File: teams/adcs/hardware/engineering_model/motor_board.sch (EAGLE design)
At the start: 80 parts

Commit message: Slight tweaks and initial board organization
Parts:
- removed BRAKE_MODE, COMMUTATION_MODE, DRIVE_ANGLE: (no value), SparkFun-Connectors:CONN_03LOCK
- removed C1: 2.2uF, rcl:C-USC1206
- removed C2, C4: 0.1uF, rcl:C-USC0805
- removed C3, C5: 1uF, rcl:C-USC1206
- removed MOTOR, MOTOR1, MOTOR2, MOTOR3: (no value), SparkFun-Connectors:CONN_08"
- removed R1, R2, R3, R4: 3.3K, rcl:R-US_R0805
- removed R5, R6, R7: 10K, rcl:R-US_R0805
- removed R8: (no value), rcl:R-US_R0805
- removed U$9: DRV10970, DubSat1 Components:DRV10970
- added MOTOR_X, MOTOR_Y, MOTOR_Z: PICOLOCK_8, DubSat1 Components:PICOLOCK_8
- renumbered BRKMOD_X1 to BRKMOD_Y, BRKMOD_X2 to BRKMOD_Z, CMTMOD_X1 to CMTMOD_Y, CMTMOD_X2 to CMTMOD_Z, DAA_X1 to DAA_Y, DAA_X2 to DAA_Z
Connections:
- removed net N$19: C1.1, U$9.RETRY
- removed net N$26: R1.1, U$9.RD
- removed net N$27: R2.2, U$9.FG
- removed net N$28: U$9.FR
- removed net N$29: C3.2, U$9.VCP
- removed net N$31: R3.2, R4.1, U$9.U_HN, U$9.V_HN, U$9.W_HN
- removed net N$32: DRIVE_ANGLE.2, U$9.DAA
- removed net N$33: COMMUTATION_MODE.2, U$9.CMTMOD
- removed net N$34: BRAKE_MODE.2, U$9.BRKMOD
- removed net N$35: BRAKE_MODE.3, C4.2, COMMUTATION_MODE.3, DRIVE_ANGLE.3, MOTOR.5, R1.2, R2.1, R4.2, R5.1, R6.1, R7.1, U$9.VINT
- removed net N$37: C2.2, U$9.CPP
- removed net N$42: C2.1, U$9.CPN
- removed net N$43: MOTOR.1, U$9.W
- removed net N$44: MOTOR.2, U$9.V
- removed net N$45: MOTOR.6, R7.2, U$9.W_HP
- removed net N$46: MOTOR.7, R6.2, U$9.V_HP
- removed net N$47: MOTOR.8, R5.2, U$9.U_HP
- removed net N$48: R8.2, U$9.CS
- removed net N$49: MOTOR.3, U$9.U
- removed net N$56: C5.2, U$9.VM
- net GND: now also MOTOR_X.P$4, MOTOR_Y.P$4, MOTOR_Z.P$4; no longer BRAKE_MODE.1, C1.2, C3.1, C4.1, C5.1, COMMUTATION_MODE.1, DRIVE_ANGLE.1, MOTOR.4, MOTOR1.4, MOTOR2.4, MOTOR3.4, R3.1, R8.1, U$9.GND
- net N$23: now also MOTOR_Y.P$1; no longer MOTOR2.1
- net N$25: now also MOTOR_Y.P$2; no longer MOTOR2.2
- net N$40: now also MOTOR_Y.P$6; no longer MOTOR2.6
- net N$41: now also MOTOR_Y.P$7; no longer MOTOR2.7
- net N$52: now also MOTOR_X.P$1; no longer MOTOR1.1
- net N$53: now also MOTOR_X.P$2; no longer MOTOR1.2
- net N$54: now also MOTOR_X.P$6; no longer MOTOR1.6
- net N$55: now also MOTOR_X.P$7; no longer MOTOR1.7
- net N$57: now also MOTOR_X.P$8; no longer MOTOR1.8
- net N$59: now also MOTOR_X.P$3; no longer MOTOR1.3
- net N$60: now also MOTOR_Y.P$8; no longer MOTOR2.8
- net N$62: now also MOTOR_Y.P$3; no longer MOTOR2.3
- net N$77: now also MOTOR_Z.P$1; no longer MOTOR3.1
- net N$78: now also MOTOR_Z.P$2; no longer MOTOR3.2
- net N$79: now also MOTOR_Z.P$6; no longer MOTOR3.6
- net N$80: now also MOTOR_Z.P$7; no longer MOTOR3.7
- net N$81: now also MOTOR_Z.P$8; no longer MOTOR3.8
- net N$83: now also MOTOR_Z.P$3; no longer MOTOR3.3
- net VINT_X: now also MOTOR_X.P$5; no longer MOTOR1.5
- net VINT_Y: now also MOTOR_Y.P$5; no longer MOTOR2.5
- net VINT_Z: now also MOTOR_Z.P$5; no longer MOTOR3.5

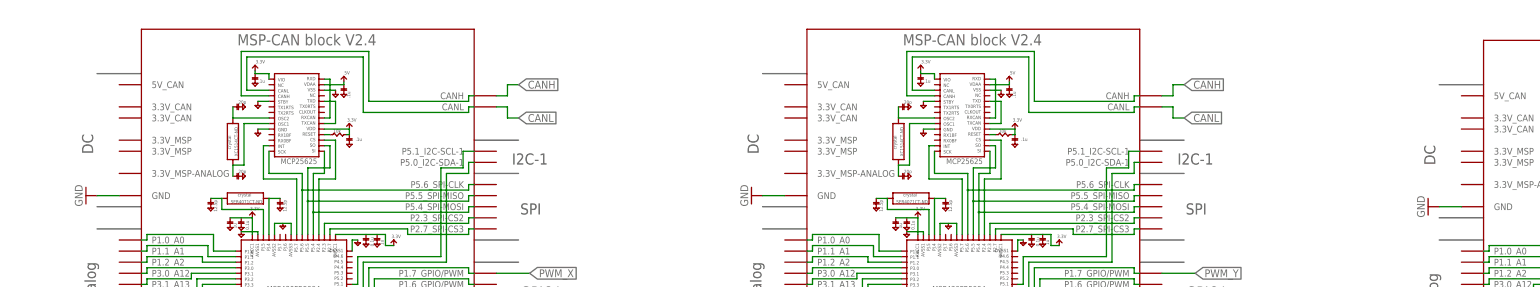
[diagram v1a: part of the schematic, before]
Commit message: ADCS/RW - Added voltage nets for MCU regulators
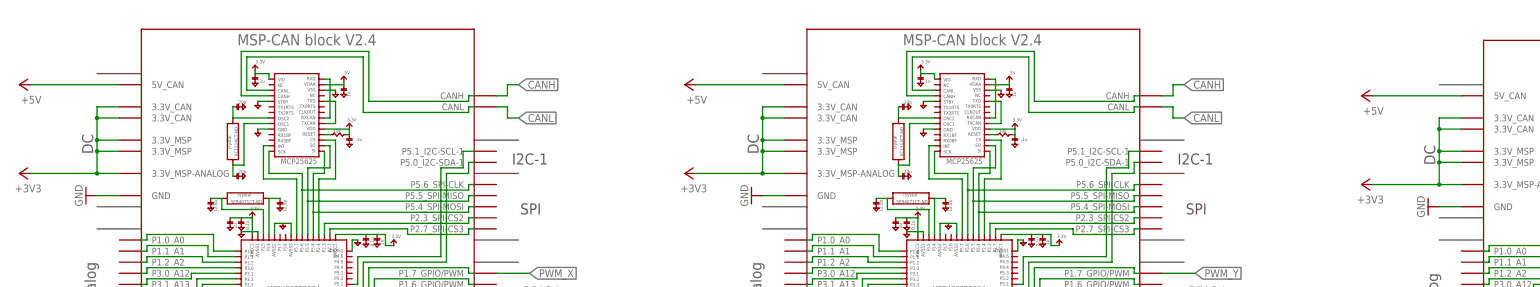
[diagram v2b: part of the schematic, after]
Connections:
- new net +3V3: U$3.3.3V_CAN@1, U$3.3.3V_CAN@2, U$3.3.3V_MSP-ANALOG@1, U$3.3.3V_MSP@2, U$3.3.3V_MSP@3
- new net +5V: U$3.5V_CAN
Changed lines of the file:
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@@
 <?xml version="1.0" encoding="utf-8"?>
 <!DOCTYPE eagle SYSTEM "eagle.dtd">
-<eagle version="8.3.1">
+<eagle version="8.3.2">
 <drawing>
 <settings>
@@
 <part name="MOTOR_Y" library="DubSat1 Components" deviceset="PICOLOCK_8" device=""/>
 <part name="MOTOR_Z" library="DubSat1 Components" deviceset="PICOLOCK_8" device=""/>
+<part name="+3V1" library="supply1" library_urn="urn:adsk.eagle:library:371" deviceset="+3V3" device=""/>
+<part name="P+1" library="supply1" library_urn="urn:adsk.eagle:library:371" deviceset="+5V" device=""/>
+<part name="+3V2" library="supply1" library_urn="urn:adsk.eagle:library:371" deviceset="+3V3" device=""/>
+<part name="P+2" library="supply1" library_urn="urn:adsk.eagle:library:371" deviceset="+5V" device=""/>
+<part name="+3V3" library="supply1" library_urn="urn:adsk.eagle:library:371" deviceset="+3V3" device=""/>
+<part name="P+3" library="supply1" library_urn="urn:adsk.eagle:library:371" deviceset="+5V" device=""/>
 </parts>
 <sheets>
@@
 <instance part="MOTOR_Y" gate="G$1" x="154.94" y="-157.48"/>
 <instance part="MOTOR_Z" gate="G$1" x="309.88" y="-160.02"/>
+<instance part="+3V1" gate="G$1" x="-63.5" y="-55.88" rot="R90"/>
+<instance part="P+1" gate="1" x="-63.5" y="-35.56" rot="R90"/>
+<instance part="+3V2" gate="G$1" x="88.9" y="-55.88" rot="R90"/>
+<instance part="P+2" gate="1" x="88.9" y="-35.56" rot="R90"/>
+<instance part="+3V3" gate="G$1" x="243.84" y="-58.42" rot="R90"/>
+<instance part="P+3" gate="1" x="243.84" y="-38.1" rot="R90"/>
 </instances>
 <busses>
@@
 </segment>
 </net>
+<net name="+3V3" class="0">
+<segment>
+<pinref part="+3V1" gate="G$1" pin="+3V3"/>
+<pinref part="U$3" gate="G$1" pin="3.3V_MSP-ANALOG@1"/>
+<wire x1="-60.96" y1="-55.88" x2="-45.72" y2="-55.88" width="0.1524" layer="91"/>
+<pinref part="U$3" gate="G$1" pin="3.3V_MSP@2"/>
+<wire x1="-45.72" y1="-55.88" x2="-40.64" y2="-55.88" width="0.1524" layer="91"/>
+<wire x1="-45.72" y1="-55.88" x2="-45.72" y2="-50.8" width="0.1524" layer="91"/>
+<wire x1="-45.72" y1="-50.8" x2="-40.64" y2="-50.8" width="0.1524" layer="91"/>
+<junction x="-45.72" y="-55.88"/>
+<pinref part="U$3" gate="G$1" pin="3.3V_MSP@3"/>
+<wire x1="-45.72" y1="-50.8" x2="-45.72" y2="-48.26" width="0.1524" layer="91"/>
+<wire x1="-45.72" y1="-48.26" x2="-40.64" y2="-48.26" width="0.1524" layer="91"/>
+<junction x="-45.72" y="-50.8"/>
+<pinref part="U$3" gate="G$1" pin="3.3V_CAN@1"/>
+<wire x1="-45.72" y1="-48.26" x2="-45.72" y2="-43.18" width="0.1524" layer="91"/>
+<wire x1="-45.72" y1="-43.18" x2="-40.64" y2="-43.18" width="0.1524" layer="91"/>
+<junction x="-45.72" y="-48.26"/>
+<pinref part="U$3" gate="G$1" pin="3.3V_CAN@2"/>
+<wire x1="-45.72" y1="-43.18" x2="-45.72" y2="-40.64" width="0.1524" layer="91"/>
+<wire x1="-45.72" y1="-40.64" x2="-40.64" y2="-40.64" width="0.1524" layer="91"/>
+<junction x="-45.72" y="-43.18"/>
+</segment>
+<segment>
+<pinref part="+3V2" gate="G$1" pin="+3V3"/>
+<wire x1="91.44" y1="-55.88" x2="106.68" y2="-55.88" width="0.1524" layer="91"/>
+<wire x1="106.68" y1="-55.88" x2="111.76" y2="-55.88" width="0.1524" layer="91"/>
+<wire x1="106.68" y1="-55.88" x2="106.68" y2="-50.8" width="0.1524" layer="91"/>
+<wire x1="106.68" y1="-50.8" x2="111.76" y2="-50.8" width="0.1524" layer="91"/>
+<junction x="106.68" y="-55.88"/>
+<wire x1="106.68" y1="-50.8" x2="106.68" y2="-48.26" width="0.1524" layer="91"/>
+<wire x1="106.68" y1="-48.26" x2="111.76" y2="-48.26" width="0.1524" layer="91"/>
+<junction x="106.68" y="-50.8"/>
+<wire x1="106.68" y1="-48.26" x2="106.68" y2="-43.18" width="0.1524" layer="91"/>
+<wire x1="106.68" y1="-43.18" x2="111.76" y2="-43.18" width="0.1524" layer="91"/>
+<junction x="106.68" y="-48.26"/>
+<wire x1="106.68" y1="-43.18" x2="106.68" y2="-40.64" width="0.1524" layer="91"/>
+<wire x1="106.68" y1="-40.64" x2="111.76" y2="-40.64" width="0.1524" layer="91"/>
+<junction x="106.68" y="-43.18"/>
+</segment>
+<segment>
+<pinref part="+3V3" gate="G$1" pin="+3V3"/>
+<wire x1="246.38" y1="-58.42" x2="261.62" y2="-58.42" width="0.1524" layer="91"/>
+<wire x1="261.62" y1="-58.42" x2="266.7" y2="-58.42" width="0.1524" layer="91"/>
+<wire x1="261.62" y1="-58.42" x2="261.62" y2="-53.34" width="0.1524" layer="91"/>
+<wire x1="261.62" y1="-53.34" x2="266.7" y2="-53.34" width="0.1524" layer="91"/>
+<junction x="261.62" y="-58.42"/>
+<wire x1="261.62" y1="-53.34" x2="261.62" y2="-50.8" width="0.1524" layer="91"/>
+<wire x1="261.62" y1="-50.8" x2="266.7" y2="-50.8" width="0.1524" layer="91"/>
+<junction x="261.62" y="-53.34"/>
+<wire x1="261.62" y1="-50.8" x2="261.62" y2="-45.72" width="0.1524" layer="91"/>
+<wire x1="261.62" y1="-45.72" x2="266.7" y2="-45.72" width="0.1524" layer="91"/>
+<junction x="261.62" y="-50.8"/>
+<wire x1="261.62" y1="-45.72" x2="261.62" y2="-43.18" width="0.1524" layer="91"/>
+<wire x1="261.62" y1="-43.18" x2="266.7" y2="-43.18" width="0.1524" layer="91"/>
+<junction x="261.62" y="-45.72"/>
+</segment>
+</net>
+<net name="+5V" class="0">
+<segment>
+<pinref part="U$3" gate="G$1" pin="5V_CAN"/>
+<pinref part="P+1" gate="1" pin="+5V"/>
+<wire x1="-40.64" y1="-35.56" x2="-60.96" y2="-35.56" width="0.1524" layer="91"/>
+</segment>
+<segment>
+<pinref part="P+2" gate="1" pin="+5V"/>
+<wire x1="111.76" y1="-35.56" x2="91.44" y2="-35.56" width="0.1524" layer="91"/>
+</segment>
+<segment>
+<pinref part="P+3" gate="1" pin="+5V"/>
+<wire x1="266.7" y1="-38.1" x2="246.38" y2="-38.1" width="0.1524" layer="91"/>
+</segment>
+</net>

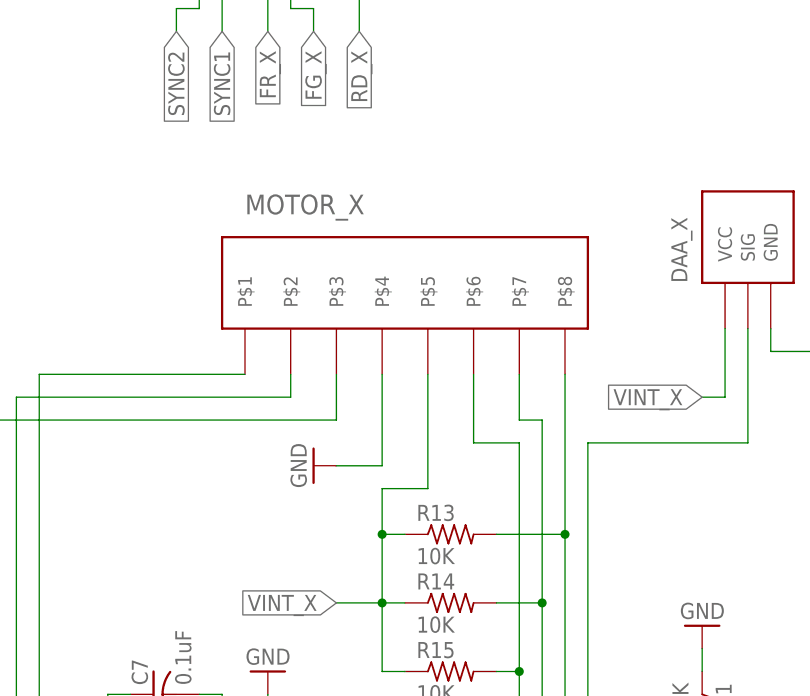
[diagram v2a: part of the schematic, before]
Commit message: ADCS/RW: Routed motor/connector region
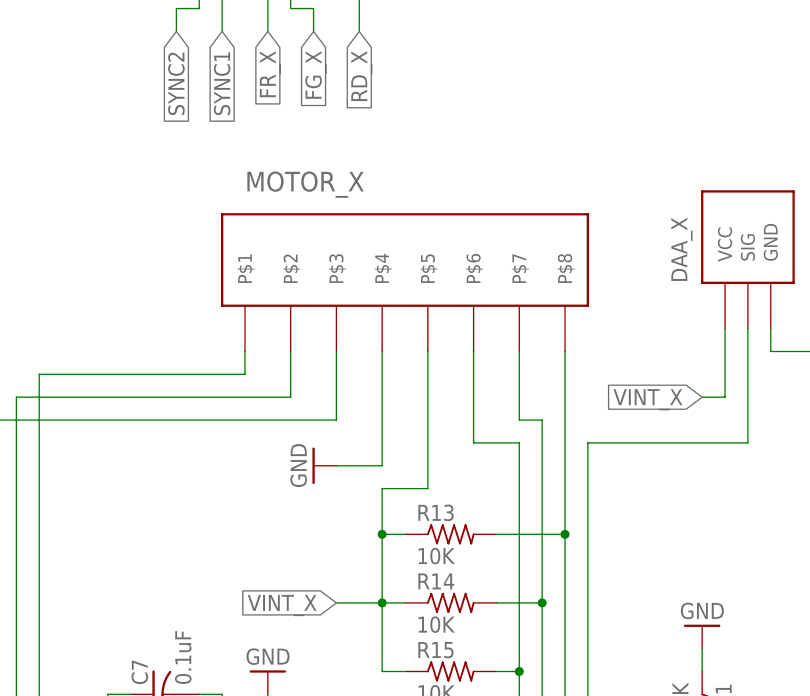
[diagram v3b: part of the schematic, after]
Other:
- moved on the sheet: MOTOR_X
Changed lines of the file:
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@@
 <instance part="DAA_Z" gate="G$1" x="350.52" y="-149.86" rot="R90"/>
 <instance part="R32" gate="G$1" x="360.68" y="-264.16" rot="R270"/>
-<instance part="MOTOR_X" gate="G$1" x="2.54" y="-162.56"/>
+<instance part="MOTOR_X" gate="G$1" x="2.54" y="-160.02"/>
 <instance part="MOTOR_Y" gate="G$1" x="154.94" y="-157.48"/>
 <instance part="MOTOR_Z" gate="G$1" x="309.88" y="-160.02"/>
@@
 <pinref part="GND25" gate="1" pin="GND"/>
 <wire x1="0" y1="-177.8" x2="5.08" y2="-177.8" width="0.1524" layer="91"/>
-<wire x1="5.08" y1="-177.8" x2="5.08" y2="-167.64" width="0.1524" layer="91"/>
+<wire x1="5.08" y1="-177.8" x2="5.08" y2="-165.1" width="0.1524" layer="91"/>
 <pinref part="MOTOR_X" gate="G$1" pin="P$4"/>
 </segment>
@@
 <pinref part="MOTOR_X" gate="G$1" pin="P$5"/>
 <wire x1="5.08" y1="-180.34" x2="10.16" y2="-180.34" width="0.1524" layer="91"/>
-<wire x1="10.16" y1="-180.34" x2="10.16" y2="-167.64" width="0.1524" layer="91"/>
+<wire x1="10.16" y1="-180.34" x2="10.16" y2="-165.1" width="0.1524" layer="91"/>
 </segment>
 <segment>
@@
 <wire x1="-33.02" y1="-167.64" x2="-10.16" y2="-167.64" width="0.1524" layer="91"/>
 <pinref part="MOTOR_X" gate="G$1" pin="P$1"/>
+<wire x1="-10.16" y1="-167.64" x2="-10.16" y2="-165.1" width="0.1524" layer="91"/>
 </segment>
 </net>
@@
 <wire x1="-27.94" y1="-261.62" x2="-35.56" y2="-261.62" width="0.1524" layer="91"/>
 <wire x1="-35.56" y1="-261.62" x2="-35.56" y2="-170.18" width="0.1524" layer="91"/>
-<wire x1="-5.08" y1="-170.18" x2="-5.08" y2="-167.64" width="0.1524" layer="91"/>
 <wire x1="-35.56" y1="-170.18" x2="-5.08" y2="-170.18" width="0.1524" layer="91"/>
 <pinref part="MOTOR_X" gate="G$1" pin="P$2"/>
+<wire x1="-5.08" y1="-170.18" x2="-5.08" y2="-165.1" width="0.1524" layer="91"/>
 </segment>
 </net>
@@
 <junction x="20.32" y="-200.66"/>
 <pinref part="MOTOR_X" gate="G$1" pin="P$6"/>
-<wire x1="15.24" y1="-167.64" x2="15.24" y2="-175.26" width="0.1524" layer="91"/>
+<wire x1="15.24" y1="-165.1" x2="15.24" y2="-175.26" width="0.1524" layer="91"/>
 </segment>
 </net>
@@
 <junction x="22.86" y="-193.04"/>
 <pinref part="MOTOR_X" gate="G$1" pin="P$7"/>
-<wire x1="20.32" y1="-167.64" x2="20.32" y2="-172.72" width="0.1524" layer="91"/>
+<wire x1="20.32" y1="-165.1" x2="20.32" y2="-172.72" width="0.1524" layer="91"/>
 </segment>
 </net>
@@
 <wire x1="25.4" y1="-210.82" x2="25.4" y2="-185.42" width="0.1524" layer="91"/>
 <wire x1="25.4" y1="-185.42" x2="17.78" y2="-185.42" width="0.1524" layer="91"/>
-<wire x1="25.4" y1="-185.42" x2="25.4" y2="-167.64" width="0.1524" layer="91"/>
+<wire x1="25.4" y1="-185.42" x2="25.4" y2="-165.1" width="0.1524" layer="91"/>
 <junction x="25.4" y="-185.42"/>
 <pinref part="MOTOR_X" gate="G$1" pin="P$8"/>
@@
 <net name="N$59" class="0">
 <segment>
-<wire x1="0" y1="-172.72" x2="0" y2="-167.64" width="0.1524" layer="91"/>
 <pinref part="U$10" gate="G$1" pin="U"/>
 <wire x1="-22.86" y1="-261.62" x2="-22.86" y2="-266.7" width="0.1524" layer="91"/>
@@
 <wire x1="0" y1="-172.72" x2="-38.1" y2="-172.72" width="0.1524" layer="91"/>
 <pinref part="MOTOR_X" gate="G$1" pin="P$3"/>
+<wire x1="0" y1="-172.72" x2="0" y2="-165.1" width="0.1524" layer="91"/>
 </segment>
 </net>
@@
 <wire x1="129.54" y1="-210.82" x2="119.38" y2="-210.82" width="0.1524" layer="91"/>
 <wire x1="119.38" y1="-210.82" x2="119.38" y2="-165.1" width="0.1524" layer="91"/>
-<wire x1="142.24" y1="-165.1" x2="142.24" y2="-162.56" width="0.1524" layer="91"/>
 <wire x1="119.38" y1="-165.1" x2="142.24" y2="-165.1" width="0.1524" layer="91"/>
 <pinref part="MOTOR_Y" gate="G$1" pin="P$1"/>
+<wire x1="142.24" y1="-165.1" x2="142.24" y2="-162.56" width="0.1524" layer="91"/>
 </segment>
 </net>
@@
 <wire x1="124.46" y1="-261.62" x2="116.84" y2="-261.62" width="0.1524" layer="91"/>
 <wire x1="116.84" y1="-261.62" x2="116.84" y2="-167.64" width="0.1524" layer="91"/>
-<wire x1="147.32" y1="-167.64" x2="147.32" y2="-162.56" width="0.1524" layer="91"/>
 <wire x1="116.84" y1="-167.64" x2="147.32" y2="-167.64" width="0.1524" layer="91"/>
 <pinref part="MOTOR_Y" gate="G$1" pin="P$2"/>
+<wire x1="147.32" y1="-167.64" x2="147.32" y2="-162.56" width="0.1524" layer="91"/>
 </segment>
 </net>
@@
 <net name="N$62" class="0">
 <segment>
-<wire x1="152.4" y1="-170.18" x2="152.4" y2="-162.56" width="0.1524" layer="91"/>
 <pinref part="U$7" gate="G$1" pin="U"/>
 <wire x1="129.54" y1="-261.62" x2="129.54" y2="-266.7" width="0.1524" layer="91"/>
@@
 <wire x1="152.4" y1="-170.18" x2="114.3" y2="-170.18" width="0.1524" layer="91"/>
 <pinref part="MOTOR_Y" gate="G$1" pin="P$3"/>
+<wire x1="152.4" y1="-170.18" x2="152.4" y2="-162.56" width="0.1524" layer="91"/>
 </segment>
 </net>
@@
 <wire x1="284.48" y1="-213.36" x2="274.32" y2="-213.36" width="0.1524" layer="91"/>
 <wire x1="274.32" y1="-213.36" x2="274.32" y2="-167.64" width="0.1524" layer="91"/>
-<wire x1="297.18" y1="-167.64" x2="297.18" y2="-165.1" width="0.1524" layer="91"/>
 <wire x1="274.32" y1="-167.64" x2="297.18" y2="-167.64" width="0.1524" layer="91"/>
 <pinref part="MOTOR_Z" gate="G$1" pin="P$1"/>
+<wire x1="297.18" y1="-167.64" x2="297.18" y2="-165.1" width="0.1524" layer="91"/>
 </segment>
 </net>
@@
 <wire x1="279.4" y1="-264.16" x2="271.78" y2="-264.16" width="0.1524" layer="91"/>
 <wire x1="271.78" y1="-264.16" x2="271.78" y2="-170.18" width="0.1524" layer="91"/>
-<wire x1="302.26" y1="-170.18" x2="302.26" y2="-165.1" width="0.1524" layer="91"/>
 <wire x1="271.78" y1="-170.18" x2="302.26" y2="-170.18" width="0.1524" layer="91"/>
 <pinref part="MOTOR_Z" gate="G$1" pin="P$2"/>
+<wire x1="302.26" y1="-170.18" x2="302.26" y2="-165.1" width="0.1524" layer="91"/>
 </segment>
 </net>
@@
 <net name="N$83" class="0">
 <segment>
-<wire x1="307.34" y1="-172.72" x2="307.34" y2="-165.1" width="0.1524" layer="91"/>
 <pinref part="U$12" gate="G$1" pin="U"/>
 <wire x1="284.48" y1="-264.16" x2="284.48" y2="-269.24" width="0.1524" layer="91"/>
@@
 <wire x1="307.34" y1="-172.72" x2="269.24" y2="-172.72" width="0.1524" layer="91"/>
 <pinref part="MOTOR_Z" gate="G$1" pin="P$3"/>
-</segment>
-</net>
+<wire x1="307.34" y1="-172.72" x2="307.34" y2="-165.1" width="0.1524" layer="91"/>
+</segment>
+</net>

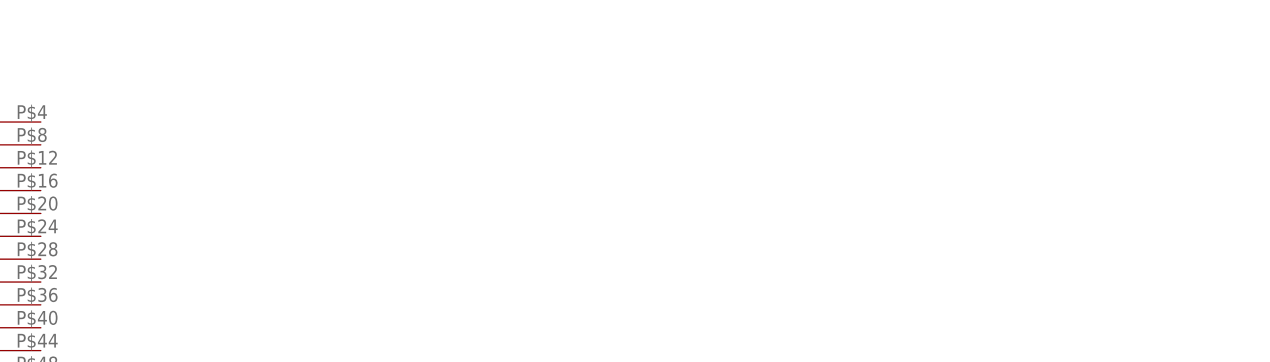
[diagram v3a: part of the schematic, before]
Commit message: ADCS/RW: Add motor bracket to drawing
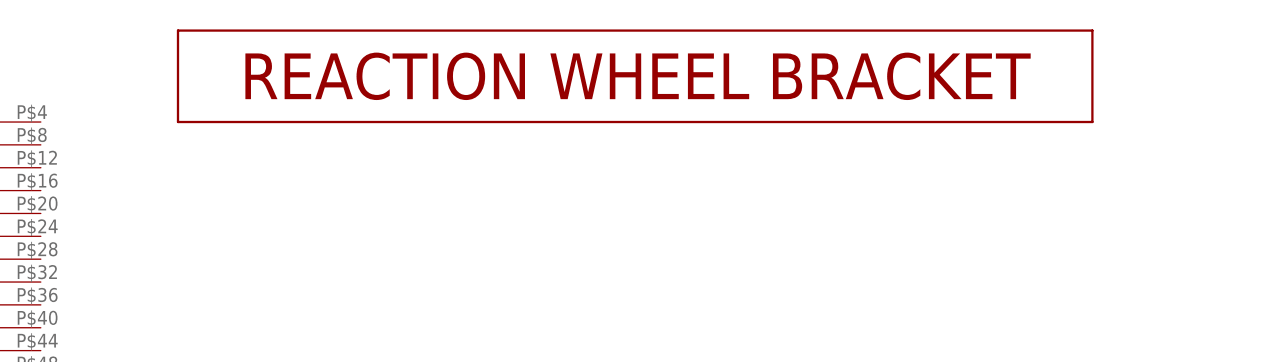
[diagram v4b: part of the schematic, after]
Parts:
- added U$9: REACTION_WHEEL_BRACKET, DubSat1 Components:REACTION_WHEEL_BRACKET
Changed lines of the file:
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@@
 <part name="+3V3" library="supply1" library_urn="urn:adsk.eagle:library:371" deviceset="+3V3" device=""/>
 <part name="P+3" library="supply1" library_urn="urn:adsk.eagle:library:371" deviceset="+5V" device=""/>
+<part name="U$9" library="DubSat1 Components" deviceset="REACTION_WHEEL_BRACKET" device=""/>
 </parts>
 <sheets>
@@
 <instance part="+3V3" gate="G$1" x="243.84" y="-58.42" rot="R90"/>
 <instance part="P+3" gate="1" x="243.84" y="-38.1" rot="R90"/>
+<instance part="U$9" gate="G$1" x="157.48" y="71.12"/>
 </instances>
 <busses>
